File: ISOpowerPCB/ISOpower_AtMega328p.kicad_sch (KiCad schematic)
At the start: 14 parts, among them J6 prog_power_select, J8 AVR-ISP-6, SW1 SW_Push, U3 ATmega328PB-M, Y1 16MHz

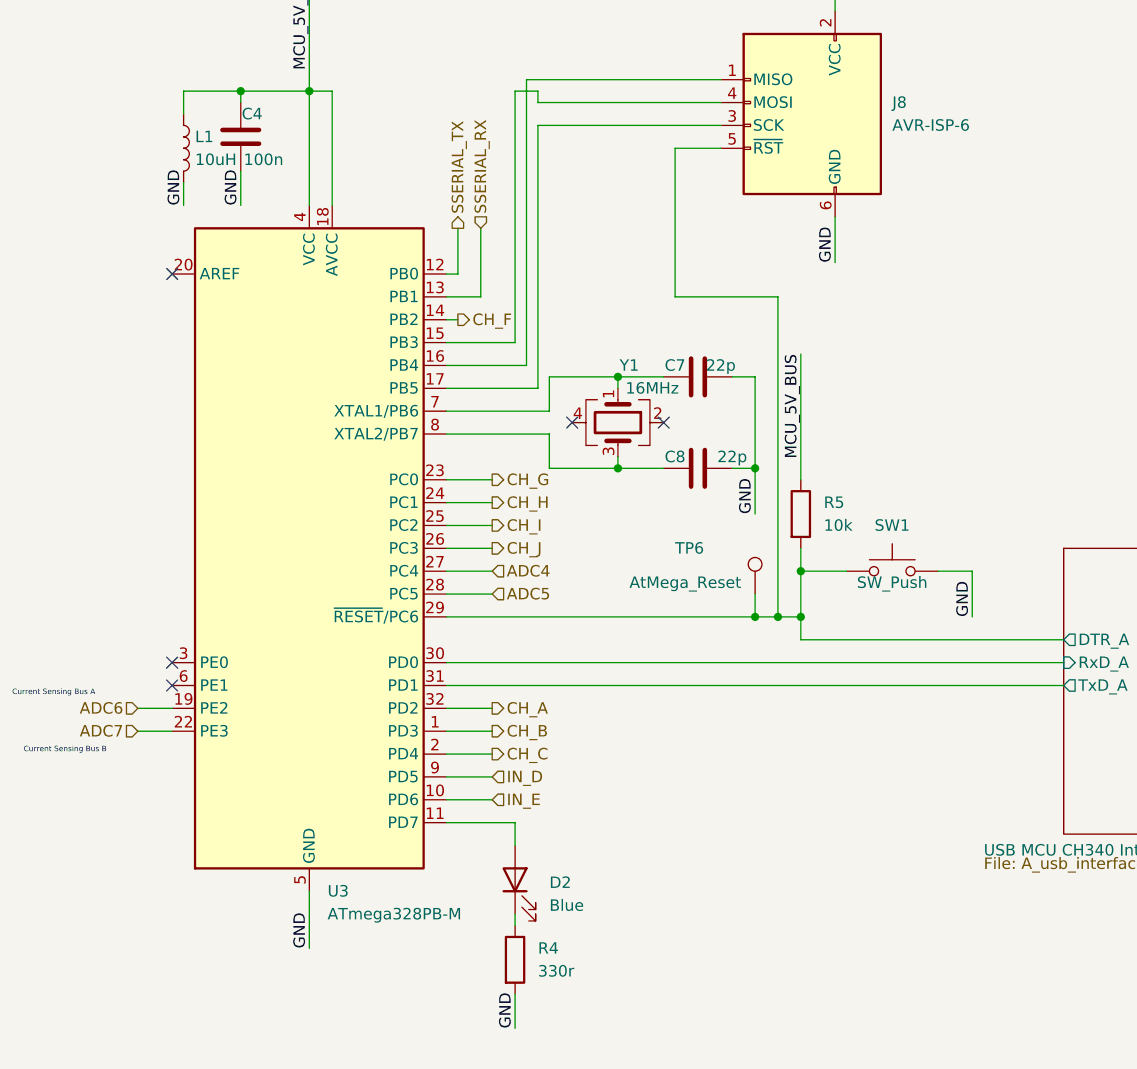
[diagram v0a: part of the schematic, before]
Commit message: PCB layout completed.
Screenshots added to media folder
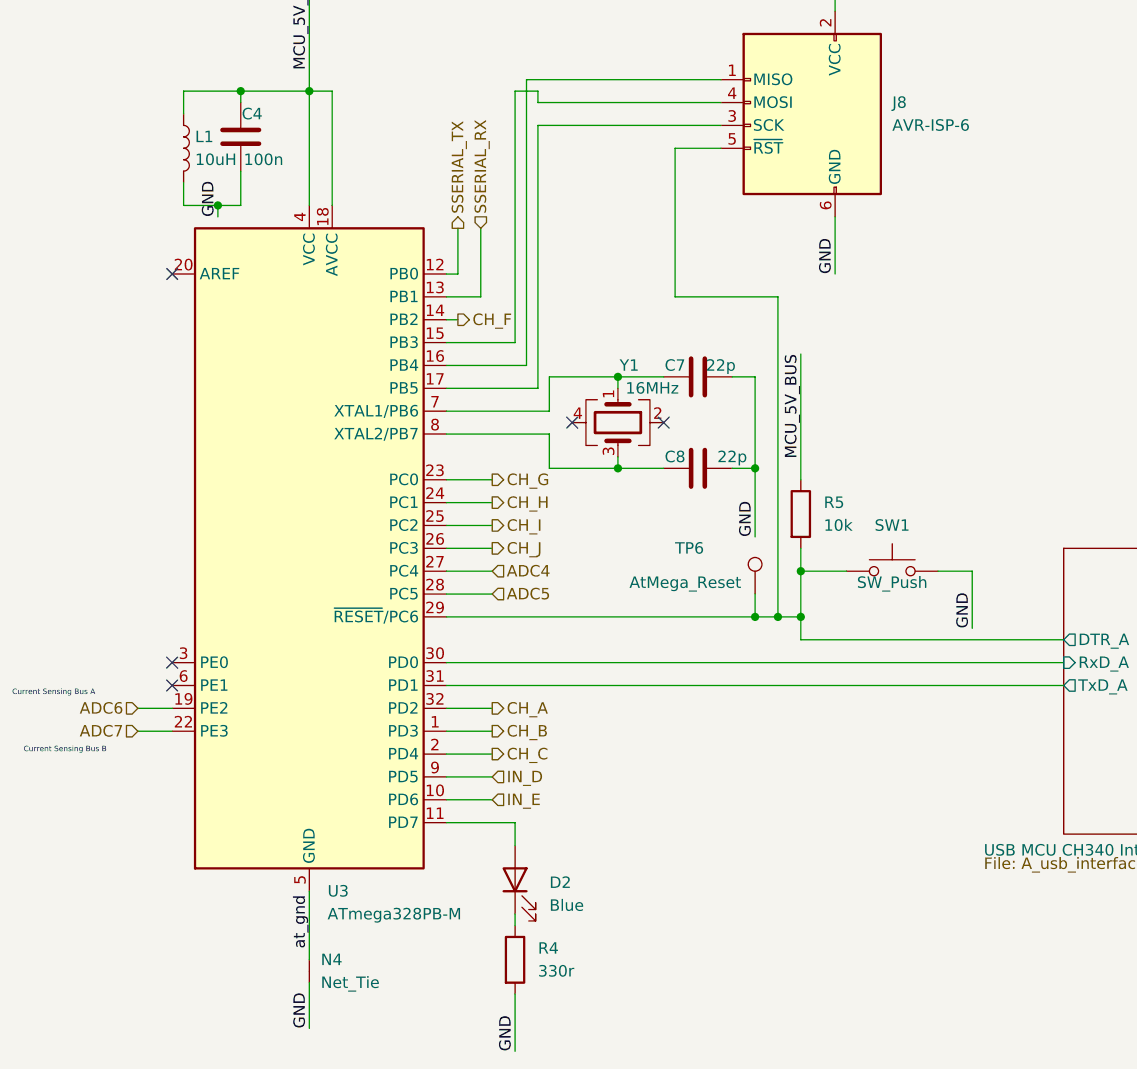
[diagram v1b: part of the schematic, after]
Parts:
- added N4: Net_Tie, NetTie:NetTie-2_SMD_Pad0.5mm, symbol 000_Utility_Immo:Net_Tie
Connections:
- net GND: now also N4.1 (A); no longer U3.21 (GND), U3.33 (GND), U3.5 (GND)
- new net at_gnd: N4.2 (C), U3.21 (GND), U3.33 (GND), U3.5 (GND)
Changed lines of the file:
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@@
   (junction (at 168.91 129.54) (diameter 0) (color 0 0 0 0)
+  )
+  (junction (at 104.14 83.82) (diameter 0) (color 0 0 0 0)
   )
   (junction (at 114.3 21.59) (diameter 0) (color 0 0 0 0)
@@
     (stroke (width 0) (type default) (color 0 0 0 0))
   )
+  (wire (pts (xy 114.3 160.02) (xy 114.3 167.64))
+    (stroke (width 0) (type default) (color 0 0 0 0))
+  )
   (wire (pts (xy 137.16 71.12) (xy 139.7 71.12))
     (stroke (width 0) (type default) (color 0 0 0 0))
@@
     (stroke (width 0) (type default) (color 0 0 0 0))
   )
-  (wire (pts (xy 106.68 80.01) (xy 106.68 83.82))
+  (wire (pts (xy 104.14 83.82) (xy 104.14 85.09))
     (stroke (width 0) (type default) (color 0 0 0 0))
   )
@@
     (stroke (width 0) (type default) (color 0 0 0 0))
   )
-  (wire (pts (xy 114.3 160.02) (xy 114.3 166.37))
-    (stroke (width 0) (type default) (color 0 0 0 0))
-  )
   (wire (pts (xy 140.97 102.87) (xy 148.59 102.87))
     (stroke (width 0) (type default) (color 0 0 0 0))
@@
     (stroke (width 0) (type default) (color 0 0 0 0))
   )
+  (wire (pts (xy 114.3 170.18) (xy 114.3 175.26))
+    (stroke (width 0) (type default) (color 0 0 0 0))
+  )
   (wire (pts (xy 129.54 129.54) (xy 163.83 129.54))
     (stroke (width 0) (type default) (color 0 0 0 0))
@@
     (stroke (width 0) (type default) (color 0 0 0 0))
   )
-  (wire (pts (xy 172.72 85.09) (xy 172.72 90.17))
+  (wire (pts (xy 172.72 85.09) (xy 172.72 91.44))
     (stroke (width 0) (type default) (color 0 0 0 0))
   )
@@
     (stroke (width 0) (type default) (color 0 0 0 0))
   )
-  (wire (pts (xy 163.83 113.03) (xy 163.83 118.11))
+  (wire (pts (xy 163.83 113.03) (xy 163.83 120.65))
     (stroke (width 0) (type default) (color 0 0 0 0))
   )
@@
     (stroke (width 0) (type default) (color 0 0 0 0))
   )
+  (wire (pts (xy 106.68 83.82) (xy 106.68 80.01))
+    (stroke (width 0) (type default) (color 0 0 0 0))
+  )
   (wire (pts (xy 129.54 142.24) (xy 134.62 142.24))
     (stroke (width 0) (type default) (color 0 0 0 0))
@@
     (stroke (width 0) (type default) (color 0 0 0 0))
   )
-  (wire (pts (xy 137.16 171.45) (xy 137.16 175.26))
-    (stroke (width 0) (type default) (color 0 0 0 0))
-  )
-  (wire (pts (xy 187.96 124.46) (xy 187.96 129.54))
+  (wire (pts (xy 137.16 171.45) (xy 137.16 177.8))
+    (stroke (width 0) (type default) (color 0 0 0 0))
+  )
+  (wire (pts (xy 187.96 124.46) (xy 187.96 130.81))
     (stroke (width 0) (type default) (color 0 0 0 0))
   )
@@
     (stroke (width 0) (type default) (color 0 0 0 0))
   )
+  (wire (pts (xy 100.33 83.82) (xy 104.14 83.82))
+    (stroke (width 0) (type default) (color 0 0 0 0))
+  )
   (wire (pts (xy 210.82 105.41) (xy 210.82 121.92))
     (stroke (width 0) (type default) (color 0 0 0 0))
@@
   )
   (wire (pts (xy 114.3 57.15) (xy 114.3 71.12))
+    (stroke (width 0) (type default) (color 0 0 0 0))
+  )
+  (wire (pts (xy 104.14 83.82) (xy 106.68 83.82))
     (stroke (width 0) (type default) (color 0 0 0 0))
   )
@@
     (effects (font (size 2 2)) (justify left bottom))
   )
-  (label "GND" (at 187.96 129.54 90)
-    (effects (font (size 1.27 1.27)) (justify left bottom))
-  )
   (label "MCU_5V_BUS" (at 82.55 25.4 0)
     (effects (font (size 1.27 1.27)) (justify left bottom))
   )
+  (label "GND" (at 114.3 175.26 90)
+    (effects (font (size 1.27 1.27)) (justify left bottom))
+  )
   (label "USB_PBUS" (at 210.82 105.41 270)
     (effects (font (size 1.27 1.27)) (justify right bottom))
   )
-  (label "GND" (at 137.16 175.26 90)
-    (effects (font (size 1.27 1.27)) (justify left bottom))
-  )
   (label "GND" (at 36.83 29.21 180)
     (effects (font (size 1.27 1.27)) (justify right bottom))
   )
-  (label "GND" (at 114.3 166.37 90)
-    (effects (font (size 1.27 1.27)) (justify left bottom))
-  )
-  (label "GND" (at 100.33 83.82 90)
+  (label "GND" (at 137.16 177.8 90)
     (effects (font (size 1.27 1.27)) (justify left bottom))
   )
@@
     (effects (font (size 1.27 1.27)) (justify left bottom))
   )
-  (label "GND" (at 163.83 118.11 90)
+  (label "GND" (at 163.83 120.65 90)
     (effects (font (size 1.27 1.27)) (justify left bottom))
   )
@@
     (effects (font (size 1.27 1.27)) (justify right bottom))
   )
+  (label "GND" (at 187.96 130.81 90)
+    (effects (font (size 1.27 1.27)) (justify left bottom))
+  )
+  (label "GND" (at 104.14 85.09 90)
+    (effects (font (size 1.27 1.27)) (justify left bottom))
+  )
+  (label "at_gnd" (at 114.3 166.37 90)
+    (effects (font (size 1.27 1.27)) (justify left bottom))
+  )
+  (label "GND" (at 172.72 91.44 90)
+    (effects (font (size 1.27 1.27)) (justify left bottom))
+  )
   (label "GND" (at 219.71 163.83 90)
     (effects (font (size 1.27 1.27)) (justify left bottom))
   )
-  (label "GND" (at 106.68 83.82 90)
-    (effects (font (size 1.27 1.27)) (justify left bottom))
-  )
-  (label "GND" (at 172.72 90.17 90)
-    (effects (font (size 1.27 1.27)) (justify left bottom))
-  )
   (label "MCU_5V_BUS" (at 219.71 105.41 270)
     (effects (font (size 1.27 1.27)) (justify right bottom))
@@
     (effects (font (size 1.27 1.27)) (justify left))
   )
+  (symbol (lib_id "000_Utility_Immo:Net_Tie") (at 114.3 168.91 90) (unit 1)
+    (in_bom no) (on_board yes) (fields_autoplaced)
+    (property "Reference" "N4" (id 0) (at 115.57 167.6399 90)
+      (effects (font (size 1.27 1.27)) (justify right))
+    )
+    (property "Value" "Net_Tie" (id 1) (at 115.57 170.1799 90)
+      (effects (font (size 1.27 1.27)) (justify right))
+    )
+    (property "Footprint" "NetTie:NetTie-2_SMD_Pad0.5mm" (id 2) (at 116.84 168.91 0)
+      (effects (font (size 1.27 1.27)) hide)
+    )
+    (property "Datasheet" "~" (id 3) (at 113.03 168.91 0)
+      (effects (font (size 1.27 1.27)) hide)
+    )
+    (pin "1")
+    (pin "2")
+  )
   (symbol (lib_id "Connector:Conn_01x03_Male") (at 128.27 25.4 180) (unit 1)
